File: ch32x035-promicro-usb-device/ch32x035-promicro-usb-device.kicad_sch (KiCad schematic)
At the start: 24 parts, among them J1 USB_TypeC-2.0_Receptacle, J2 SWD_10Pin_MCU-Side, SW1 SW_Push, U1 AMS1117-3.3, U2 CH32X035G8U6, U3 CH217K

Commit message: ch32x035-usb-device
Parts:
- J1: value USB_TypeC-2.0_Receptacle -> 217179-0001
- SW1: value SW_Push -> SKRPABE010
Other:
- note added: "SWD"
- note removed: "RESET"
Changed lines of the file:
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@@
     (effects (font (size 2.54 2.54)) (justify left bottom))
   )
-  (text "RESET" (at 111.76 113.03 0)
+  (text "SWD" (at 111.76 113.03 0)
     (effects (font (size 2.54 2.54)) (justify left bottom))
   )
@@
       (effects (font (size 1.27 1.27)) (justify left))
     )
-    (property "Value" "SW_Push" (at 172.72 121.92 90)
+    (property "Value" "SKRPABE010" (at 172.72 121.92 90)
       (effects (font (size 1.27 1.27)) (justify left))
     )
@@
       (effects (font (size 1.27 1.27)))
     )
-    (property "Value" "USB_TypeC-2.0_Receptacle" (at 194.31 27.94 0)
+    (property "Value" "217179-0001" (at 194.31 27.94 0)
       (effects (font (size 1.27 1.27)))
     )
@@
       (effects (font (size 1.27 1.27)) (justify left))
     )
-    (property "Value" "ProMicro-Left_NoGND" (at 31.75 119.38 0)
-      (effects (font (size 1.27 1.27)) (justify left))
-    )
+    (property "Value" "ProMicro-Left_NoGND" (at 29.21 119.38 0)
+      (effects (font (size 1.27 1.27)) (justify left))
+    )

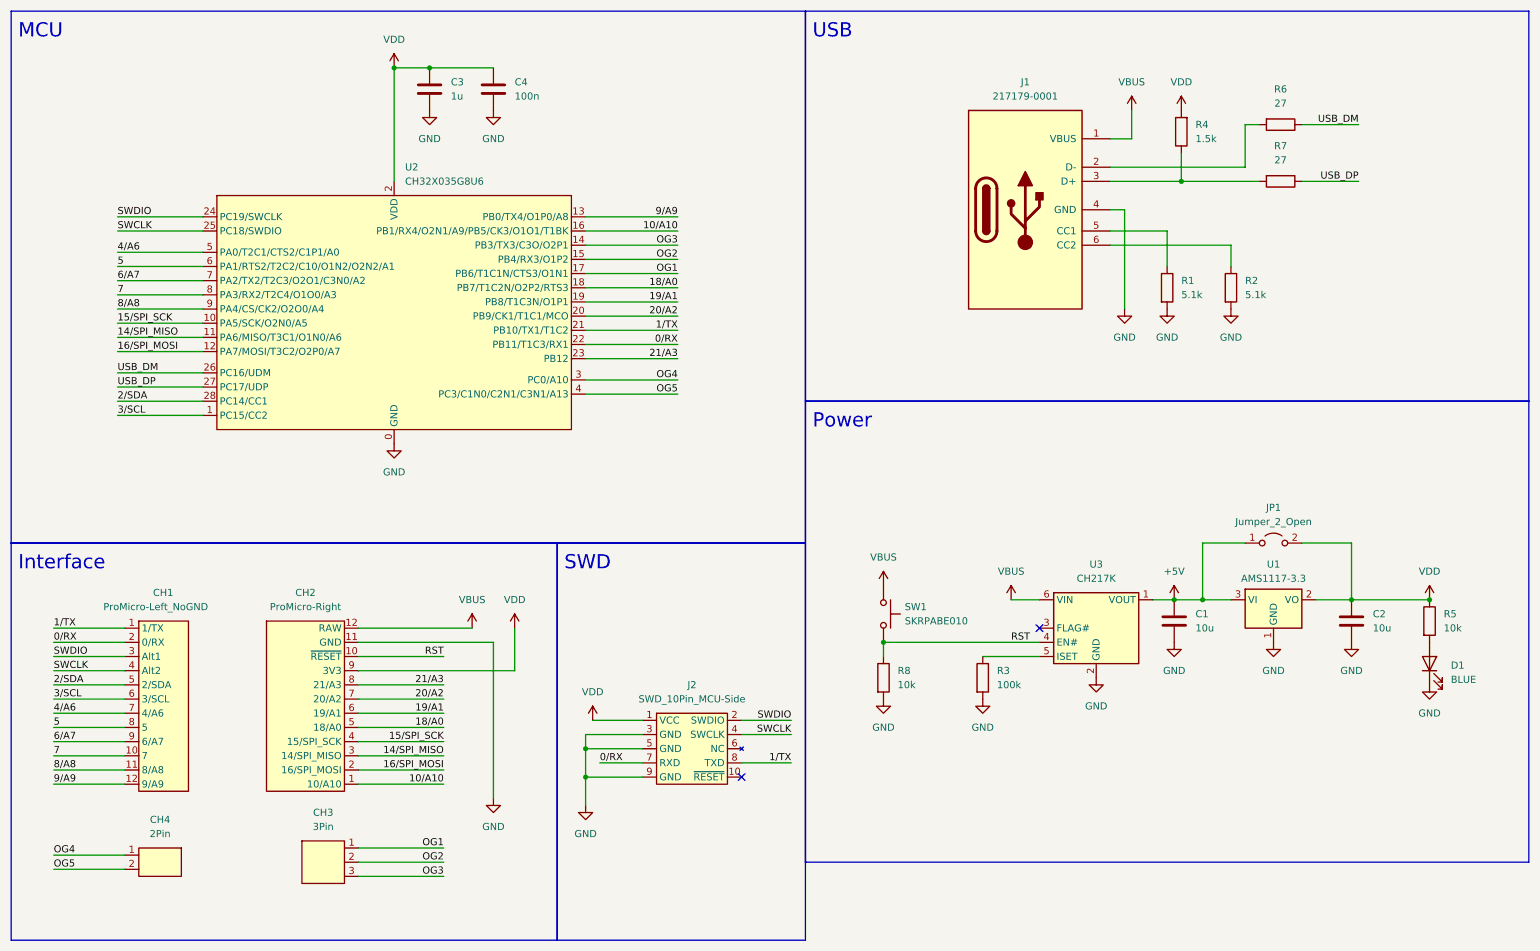
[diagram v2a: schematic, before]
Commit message: fix SWDIO/SWCLK
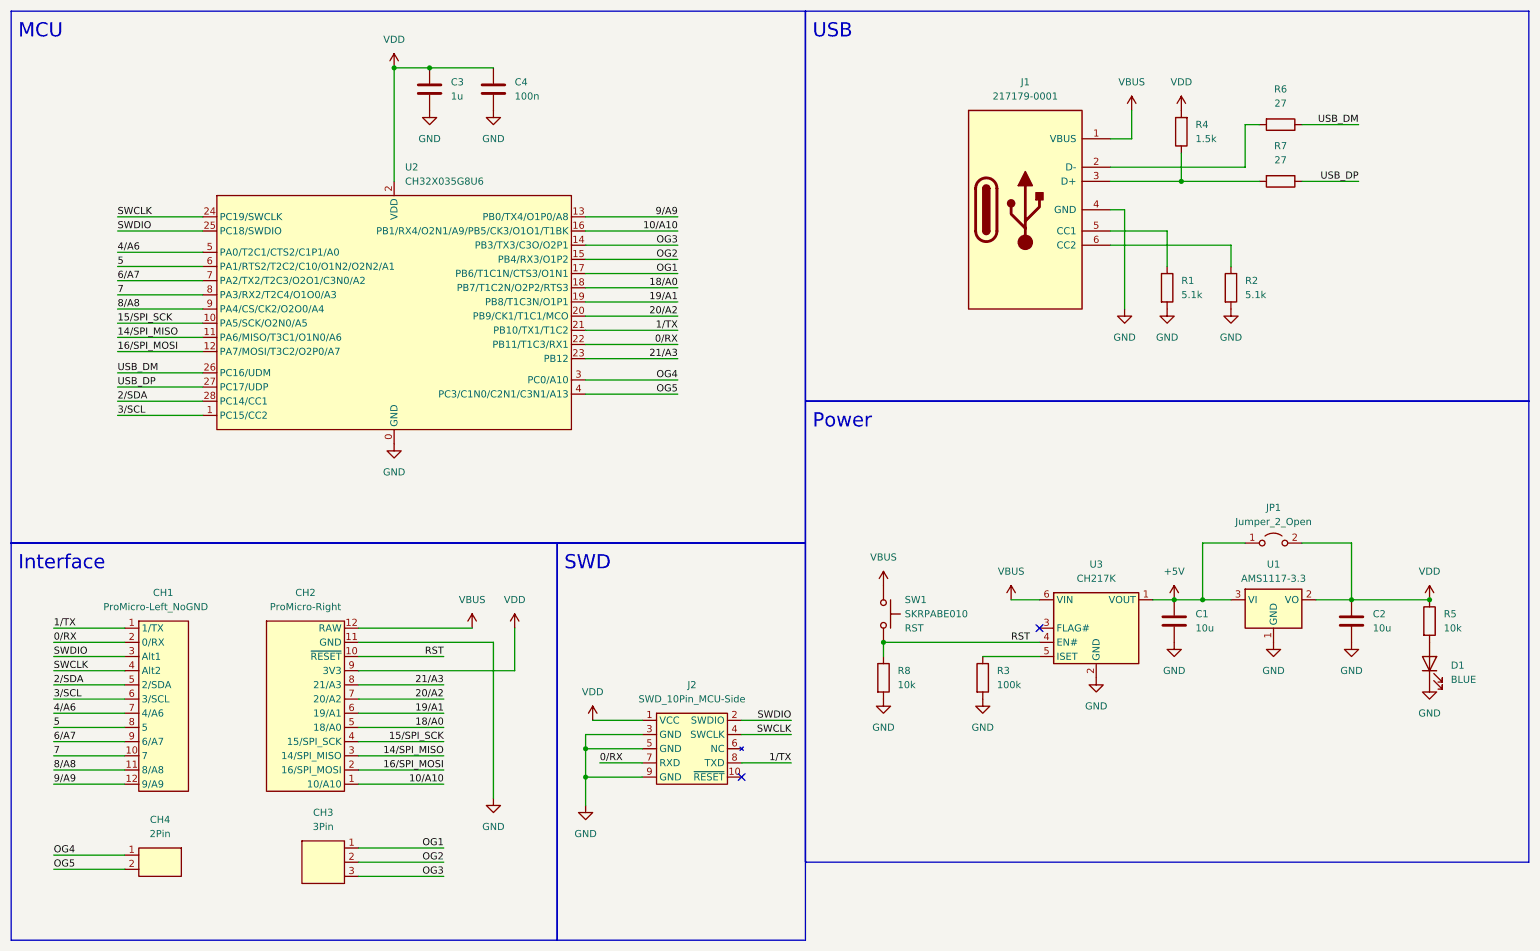
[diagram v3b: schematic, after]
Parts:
- SW1: symbol Switch:SW_Push -> 74th_Interface:SW_SKRPABE010; Function (none) -> RST
- U2: footprint 74th:QFN-28-1EP_4x4mm_P0.4mm_EP2.8x2.8mm -> 74th:Package_QFN-28-1EP_4x4mm_P0.4mm_EP2.8x2.8mm
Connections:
- net SWCLK: now also U2.24 (PC19/SWCLK); no longer U2.25 (PC18/SWDIO)
- net SWDIO: now also U2.25 (PC18/SWDIO); no longer U2.24 (PC19/SWCLK)
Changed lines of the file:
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@@
     (title "ch32x035 ProMicro")
     (date "2023-09-18")
-    (rev "1.0.0")
+    (rev "1.0.1")
     (company "@74th")
   )
@@
     (effects (font (size 1.27 1.27)) (justify right bottom))
   )
-  (label "SWDIO" (at 31.75 49.53 0) (fields_autoplaced)
+  (label "SWDIO" (at 31.75 52.07 0) (fields_autoplaced)
     (effects (font (size 1.27 1.27)) (justify left bottom))
   )
@@
     (effects (font (size 1.27 1.27)) (justify left bottom))
   )
-  (label "SWCLK" (at 31.75 52.07 0) (fields_autoplaced)
+  (label "SWCLK" (at 31.75 49.53 0) (fields_autoplaced)
     (effects (font (size 1.27 1.27)) (justify left bottom))
   )
@@
     )
   )
-  (symbol (lib_id "Switch:SW_Push") (at 168.91 120.65 270) (unit 1)
-    (in_bom yes) (on_board yes) (dnp no) (fields_autoplaced)
-    (property "Reference" "SW1" (at 172.72 119.38 90)
-      (effects (font (size 1.27 1.27)) (justify left))
-    )
-    (property "Value" "SKRPABE010" (at 172.72 121.92 90)
+  (symbol (lib_id "74th_Interface:SW_SKRPABE010") (at 168.91 120.65 270) (unit 1)
+    (in_bom yes) (on_board yes) (dnp no) (fields_autoplaced)
+    (property "Reference" "SW1" (at 172.72 118.11 90)
+      (effects (font (size 1.27 1.27)) (justify left))
+    )
+    (property "Value" "SKRPABE010" (at 172.72 120.65 90)
       (effects (font (size 1.27 1.27)) (justify left))
     )
@@
     (property "Datasheet" "~" (at 173.99 120.65 0)
       (effects (font (size 1.27 1.27)) hide)
+    )
+    (property "Function" "RST" (at 172.72 123.19 90)
+      (effects (font (size 1.27 1.27)) (justify left))
     )
     (pin "1")
@@
       (effects (font (size 1.27 1.27)) (justify left))
     )
-    (property "Footprint" "74th:QFN-28-1EP_4x4mm_P0.4mm_EP2.8x2.8mm" (at 81.28 29.21 0)
-      (effects (font (size 1.27 1.27)) hide)
-    )
+    (property "Footprint" "74th:Package_QFN-28-1EP_4x4mm_P0.4mm_EP2.8x2.8mm" (at 81.28 29.21 0)
+      (effects (font (size 1.27 1.27)) hide)
+    )

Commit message: update
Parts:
- R3: value 100k -> 56k
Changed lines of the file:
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@@
       (effects (font (size 1.27 1.27)) (justify left))
     )
-    (property "Value" "100k" (at 189.23 133.35 0)
+    (property "Value" "56k" (at 189.23 133.35 0)
       (effects (font (size 1.27 1.27)) (justify left))
     )
